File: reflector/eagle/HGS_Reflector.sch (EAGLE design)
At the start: 27 parts, among them J1 U.FL, U3 LP2985XX-N

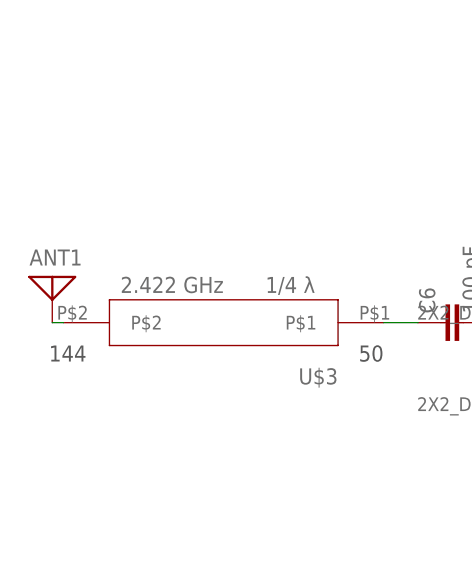
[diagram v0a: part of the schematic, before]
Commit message: Fixed keepout zones, removed antenna through hole, put 1/4 wave transformer in the right place, but, this is going to be totally hoky. Is there a better way?
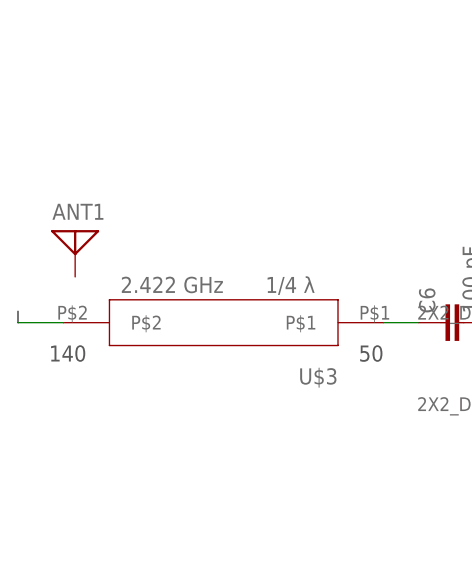
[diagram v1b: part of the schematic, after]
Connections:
- net N$2: no longer ANT1.1
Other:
- moved on the sheet: ANT1
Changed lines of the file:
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@@
 <?xml version="1.0" encoding="utf-8"?>
 <!DOCTYPE eagle SYSTEM "eagle.dtd">
-<eagle version="9.6.2">
+<eagle version="9.6.1">
 <drawing>
 <settings>
-<setting alwaysvectorfont="yes"/>
+<setting alwaysvectorfont="no"/>
 <setting verticaltext="up"/>
 </settings>
-<grid distance="0.05" unitdist="inch" unit="inch" style="lines" multiple="1" display="yes" altdistance="0.01" altunitdist="inch" altunit="inch"/>
+<grid distance="0.1" unitdist="inch" unit="inch" style="lines" multiple="1" display="no" altdistance="0.01" altunitdist="inch" altunit="inch"/>
 <layers>
 <layer number="1" name="Top" color="4" fill="1" visible="no" active="no"/>
@@
 <attribute name="VALUE" x="82.55" y="88.9" size="1.778" layer="96"/>
 </instance>
-<instance part="ANT1" gate="A" x="31.75" y="118.11" smashed="yes">
-<attribute name="NAME" x="29.21" y="119.38" size="1.778" layer="95"/>
-<attribute name="VALUE" x="34.29" y="113.03" size="1.778" layer="96"/>
+<instance part="ANT1" gate="A" x="34.29" y="123.19" smashed="yes">
+<attribute name="NAME" x="31.75" y="124.46" size="1.778" layer="95"/>
+<attribute name="VALUE" x="36.83" y="118.11" size="1.778" layer="96"/>
 </instance>
 <instance part="LED1" gate="G$1" x="101.6" y="179.07" smashed="yes">
@@
 <pinref part="L1" gate="G$1" pin="2"/>
 <wire x1="200.66" y1="138.43" x2="200.66" y2="137.16" width="0.1524" layer="91"/>
-</segment>
-</net>
-<net name="N$2" class="0">
-<segment>
-<pinref part="ANT1" gate="A" pin="1"/>
-<pinref part="U$3" gate="G$1" pin="P$2"/>
-<wire x1="31.75" y1="113.03" x2="33.02" y2="113.03" width="0.1524" layer="91"/>
 </segment>
 </net>
@@
 </segment>
 </net>
+<net name="N$2" class="0">
+<segment>
+<pinref part="U$3" gate="G$1" pin="P$2"/>
+<wire x1="33.02" y1="113.03" x2="27.94" y2="113.03" width="0.1524" layer="91"/>
+<wire x1="27.94" y1="113.03" x2="27.94" y2="114.3" width="0.1524" layer="91"/>
+</segment>
+</net>

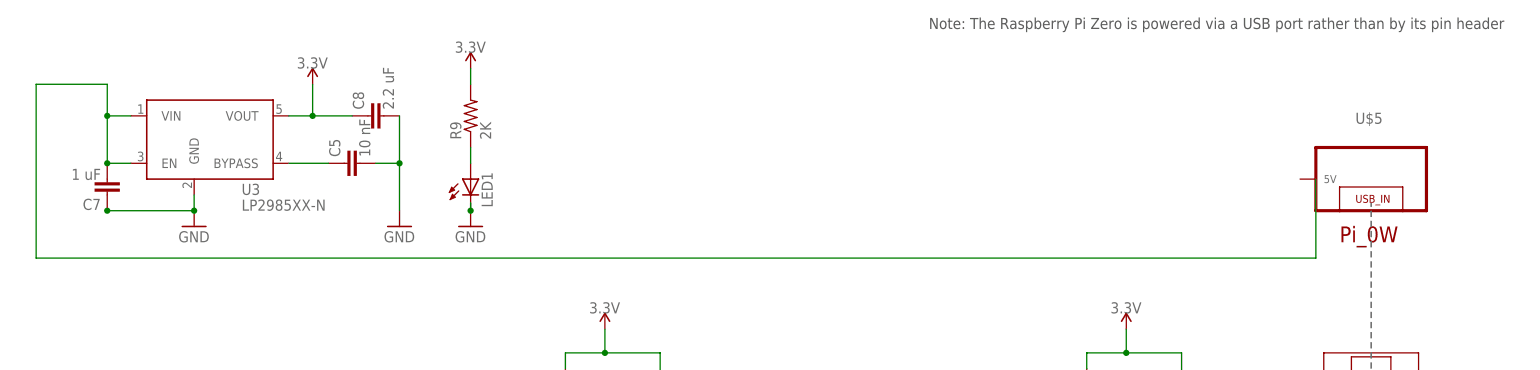
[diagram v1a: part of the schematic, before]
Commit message: After connecting the Pi 0W footprint to the ground plane, I fixed the issue of the Pi 0W pin header floating.
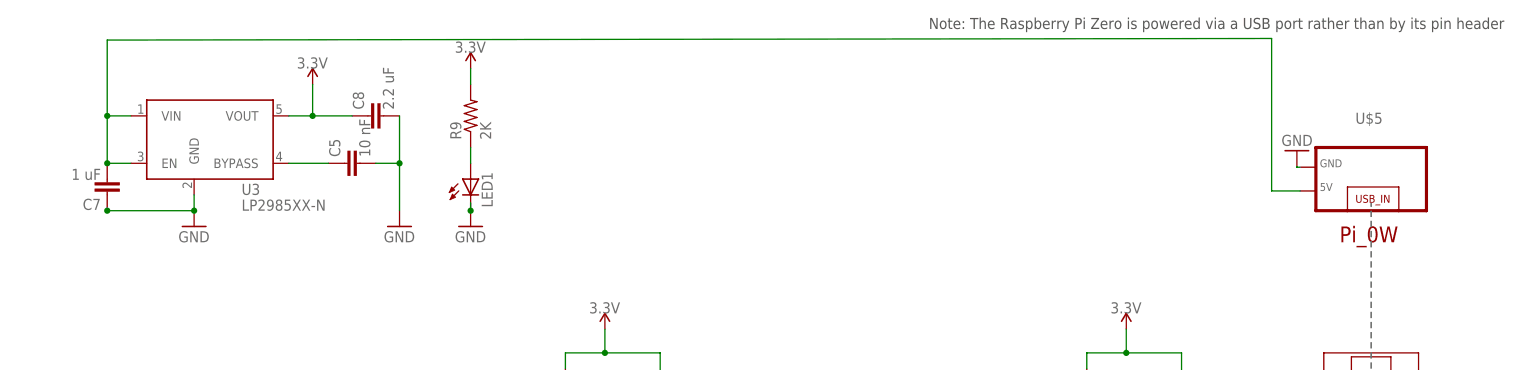
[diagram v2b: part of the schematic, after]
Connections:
- net GND: now also U$5.GND
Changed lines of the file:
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@@
 <?xml version="1.0" encoding="utf-8"?>
 <!DOCTYPE eagle SYSTEM "eagle.dtd">
-<eagle version="9.6.1">
+<eagle version="9.6.2">
 <drawing>
 <settings>
-<setting alwaysvectorfont="no"/>
+<setting alwaysvectorfont="yes"/>
 <setting verticaltext="up"/>
 </settings>
-<grid distance="0.1" unitdist="inch" unit="inch" style="lines" multiple="1" display="no" altdistance="0.01" altunitdist="inch" altunit="inch"/>
+<grid distance="0.01" unitdist="inch" unit="inch" style="lines" multiple="1" display="yes" altdistance="0.01" altunitdist="inch" altunit="inch"/>
 <layers>
 <layer number="1" name="Top" color="4" fill="1" visible="no" active="no"/>
@@
 <part name="C5" library="oresat-rcl" deviceset="C-EU" device="0402-C-NOSILK" value="10 nF"/>
 <part name="C8" library="oresat-rcl" deviceset="C-EU" device="0402-C-NOSILK" value="2.2 uF"/>
+<part name="GND10" library="supply1" library_urn="urn:adsk.eagle:library:371" deviceset="GND" device=""/>
 </parts>
 <sheets>
@@
 <attribute name="VALUE" x="89.281" y="190.246" size="1.778" layer="96" rot="R90"/>
 </instance>
+<instance part="GND10" gate="1" x="234.442" y="183.642" smashed="yes" rot="R180">
+<attribute name="VALUE" x="236.982" y="186.182" size="1.778" layer="96" rot="R180"/>
+</instance>
 </instances>
 <busses>
@@
 <wire x1="90.17" y1="181.61" x2="86.36" y2="181.61" width="0.1524" layer="91"/>
 <junction x="90.17" y="181.61"/>
+</segment>
+<segment>
+<pinref part="U$5" gate="G$1" pin="GND"/>
+<pinref part="GND10" gate="1" pin="GND"/>
+<wire x1="234.95" y1="180.975" x2="234.442" y2="180.975" width="0.1524" layer="91"/>
+<wire x1="234.442" y1="180.975" x2="234.442" y2="181.102" width="0.1524" layer="91"/>
 </segment>
 </net>
@@
 </segment>
 </net>
-<net name="N$12" class="1">
+<net name="N$2" class="0">
+<segment>
+<pinref part="U$3" gate="G$1" pin="P$2"/>
+<wire x1="33.02" y1="113.03" x2="27.94" y2="113.03" width="0.1524" layer="91"/>
+<wire x1="27.94" y1="113.03" x2="27.94" y2="114.3" width="0.1524" layer="91"/>
+</segment>
+</net>
+<net name="N$15" class="1">
 <segment>
 <pinref part="U3" gate="G$1" pin="VIN"/>
 <wire x1="46.99" y1="189.23" x2="43.18" y2="189.23" width="0.1524" layer="91"/>
+<junction x="43.18" y="189.23"/>
 <wire x1="43.18" y1="181.61" x2="43.18" y2="189.23" width="0.1524" layer="91"/>
 <pinref part="U3" gate="G$1" pin="EN"/>
 <wire x1="46.99" y1="181.61" x2="43.18" y2="181.61" width="0.1524" layer="91"/>
-<wire x1="43.18" y1="189.23" x2="43.18" y2="194.31" width="0.1524" layer="91"/>
-<junction x="43.18" y="189.23"/>
 <pinref part="C7" gate="CE" pin="2"/>
 <junction x="43.18" y="181.61"/>
-<wire x1="43.18" y1="194.31" x2="31.75" y2="194.31" width="0.1524" layer="91"/>
-<wire x1="31.75" y1="194.31" x2="31.75" y2="166.37" width="0.1524" layer="91"/>
+<wire x1="43.18" y1="201.422" x2="230.378" y2="201.676" width="0.1524" layer="91"/>
+<wire x1="43.18" y1="189.23" x2="43.18" y2="201.422" width="0.1524" layer="91"/>
 <pinref part="U$5" gate="G$1" pin="5V"/>
-<wire x1="31.75" y1="166.37" x2="237.49" y2="166.37" width="0.1524" layer="91"/>
-<wire x1="237.49" y1="166.37" x2="237.49" y2="179.07" width="0.1524" layer="91"/>
-</segment>
-</net>
-<net name="N$2" class="0">
-<segment>
-<pinref part="U$3" gate="G$1" pin="P$2"/>
-<wire x1="33.02" y1="113.03" x2="27.94" y2="113.03" width="0.1524" layer="91"/>
-<wire x1="27.94" y1="113.03" x2="27.94" y2="114.3" width="0.1524" layer="91"/>
-</segment>
-</net>
+<wire x1="230.378" y1="201.676" x2="230.378" y2="177.165" width="0.1524" layer="91"/>
+<wire x1="230.378" y1="177.165" x2="234.95" y2="177.165" width="0.1524" layer="91"/>
+</segment>
+</net>

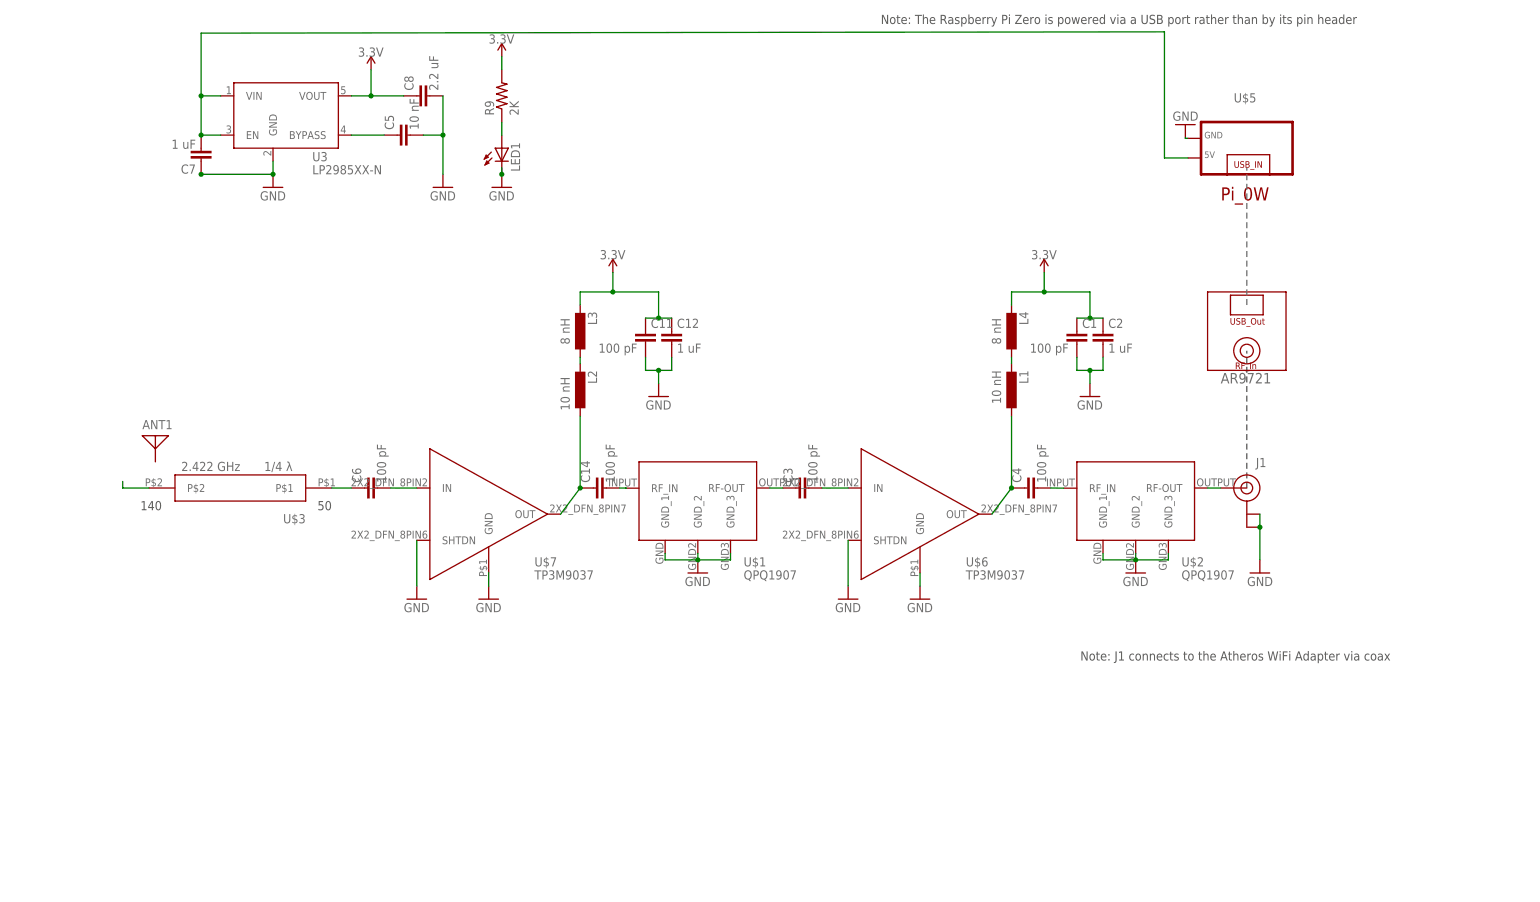
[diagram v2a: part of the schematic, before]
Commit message: Design review of HGS - moving towards Oliver's power distribution ideas from 12/14.
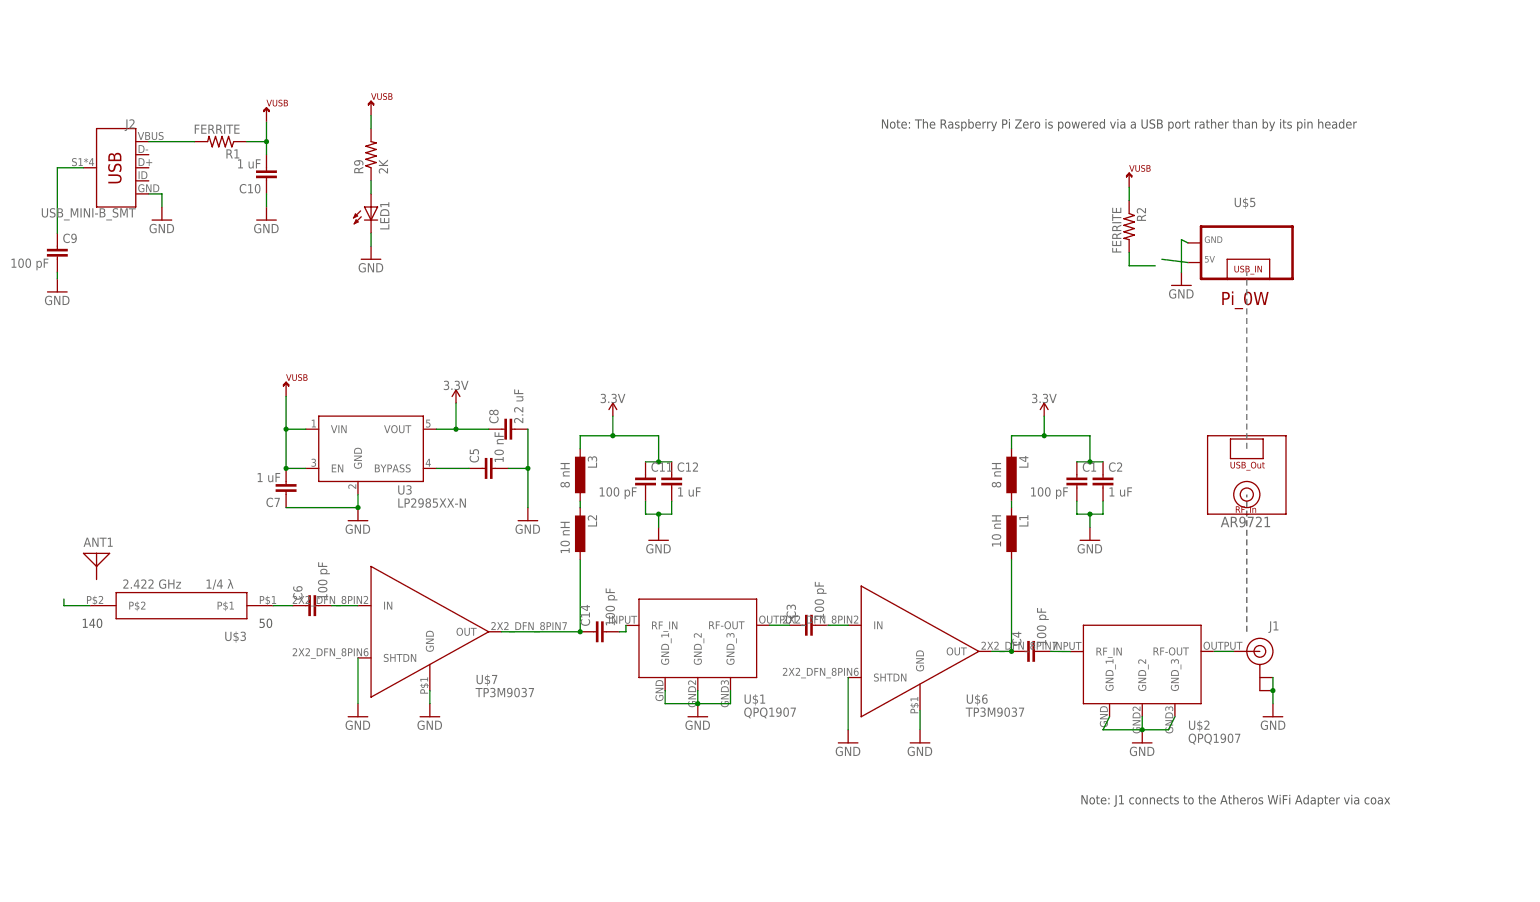
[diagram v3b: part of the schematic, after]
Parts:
- added C10: 1 uF, oresat-rcl:C-EU0402-C-NOSILK
- added C9: 100 pF, oresat-rcl:C-EU0603-C-NOSILK
- added J2: USB_MINI-B_SMT, SparkFun-Connectors:USB_MINI-B_SMT
- added R1, R2: FERRITE, oresat-rcl:R-US_0603-C-NOSILK
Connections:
- new net N$12: C9.1, J2.SHIELD
- new net N$17: J2.VBUS, R1.2
- new net N$18: R2.2
- new net VUSB: C10.2, C7.2, R1.1, R2.1, R9.2, U3.EN, U3.VIN
- net 3.3V: no longer R9.2
- net GND: now also C10.1, C9.2, J2.GND
- net N$15: no longer C7.2, U3.EN, U3.VIN
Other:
- moved on the sheet: ANT1, C1, C11, C12, C14, C2, C3, C4, C5, C6, C7, C8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

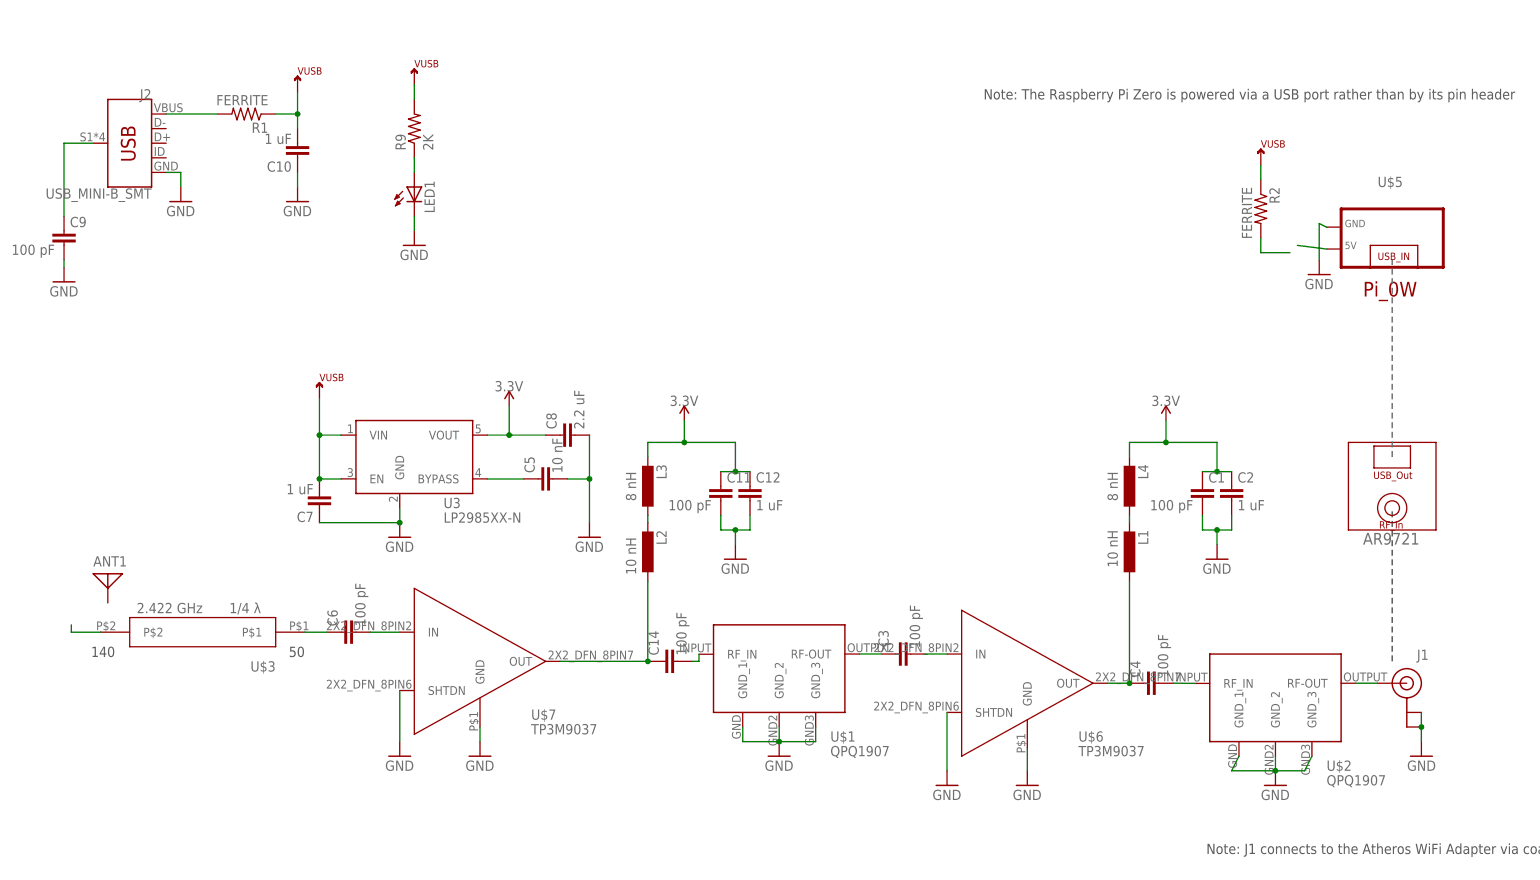
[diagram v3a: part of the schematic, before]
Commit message: After modifying the schematic symbol in the ferrite bead library, I updated the HGS schematic to match Oliver Jones' power distribution block diagram.
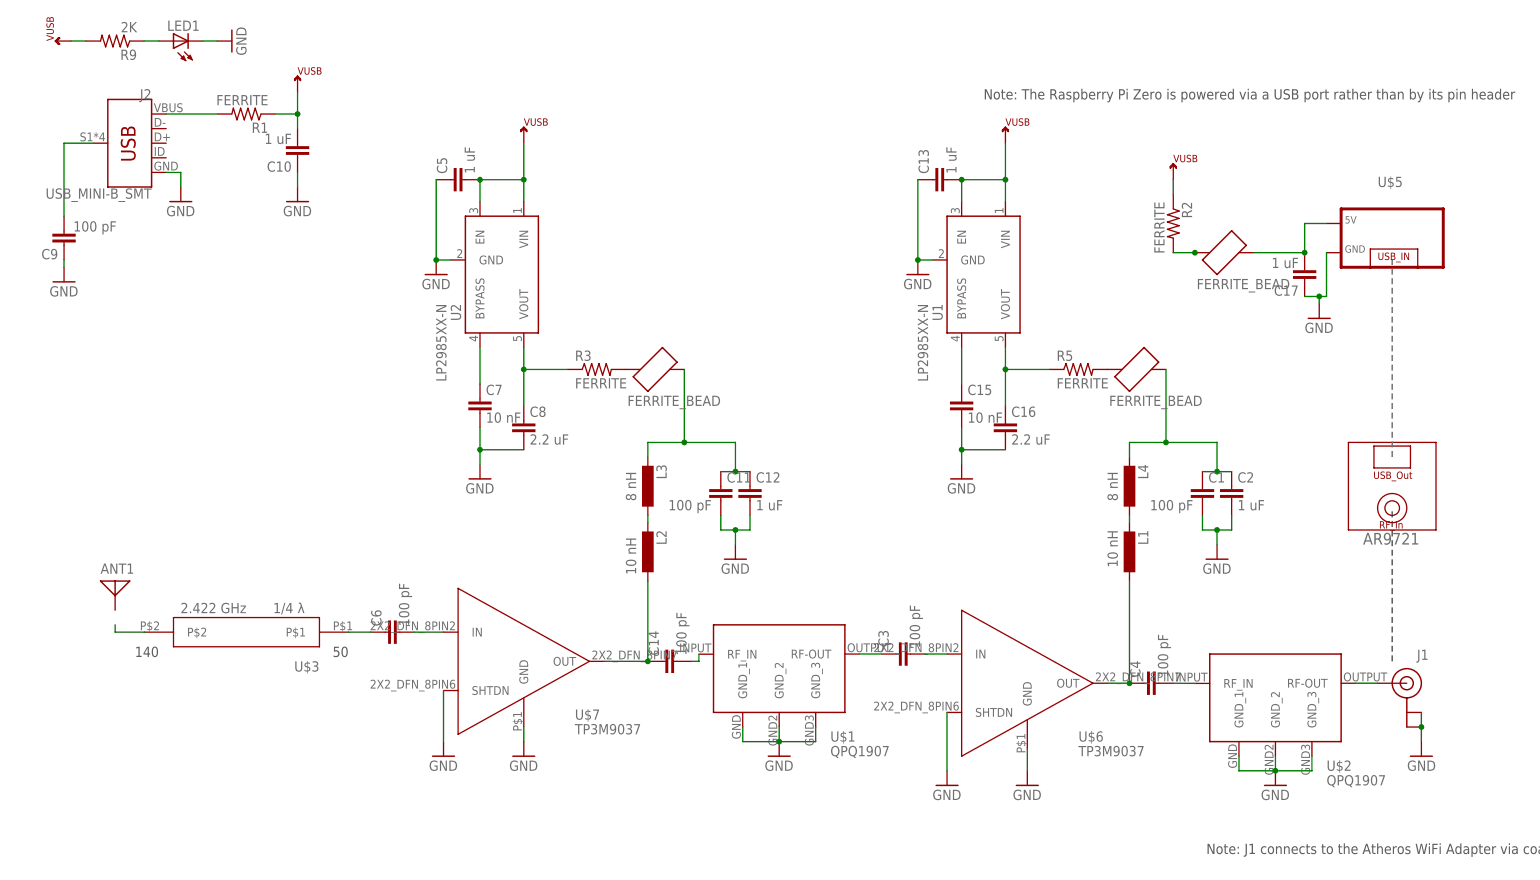
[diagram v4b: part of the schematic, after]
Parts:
- removed U3: LP2985XX-N, U-TI-LP2985XX-N-linear-reg:LP2985XX-N
- added C13, C17: 1 uF, oresat-rcl:C-EU0402-C-NOSILK
- added C15: 10 nF, oresat-rcl:C-EU0402-C-NOSILK
- added C16: 2.2 uF, oresat-rcl:C-EU0402-C-NOSILK
- added R3, R5: FERRITE, oresat-rcl:R-US_0603-C-NOSILK
- added U$10, U$8, U$9: FERRITE_BEAD, Ferrite Bead:FERRITE_BEAD
- added U1, U2: LP2985XX-N, U-TI-LP2985XX-N-linear-reg:LP2985XX-N
- C5: value 10 nF -> 1 uF
- C7: value 1 uF -> 10 nF
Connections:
- removed net 3.3V: C1.1, C11.1, C12.1, C2.1, C8.1, L3.2, L4.2, U3.VOUT
- new net N$19: C15.1, U1.BYPASS
- new net N$20: C11.1, C12.1, L3.2, U$9.P$3
- new net N$21: C1.1, C2.1, L4.2, U$8.P$3
- new net N$22: C16.1, R5.1, U1.VOUT
- new net N$25: C8.1, R3.1, U2.VOUT
- net GND: now also C13.1, C15.2, C16.2, C17.1, C5.1, C7.2, C9.1, U1.GND, U2.GND; no longer C5.2, C7.1, C9.2, U3.GND
- net N$1: now also C7.1, U2.BYPASS; no longer C5.1, U3.BYPASS
- net N$12: now also C9.2; no longer C9.1
- net N$15: now also C17.2, U$10.P$3
- net N$18: now also U$10.P$1
- net VUSB: now also C13.2, C5.2, U1.EN, U1.VIN, U2.EN, U2.VIN; no longer C7.2, U3.EN, U3.VIN
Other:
- moved on the sheet: ANT1, C5, C6, C7, C8, C9, LED1, R2, R9, U$3, U$7
